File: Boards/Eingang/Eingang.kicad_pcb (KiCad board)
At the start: 2 copper layers, 9 parts, among them P1 CONN_01X02, P2 CONN_01X02, P3 CONN_01X02, P4 CONN_01X03, P5 CONN_01X03, P6 CONN_01X03, P7 CONN_01X02, P8 CONN_01X02, P9 CONN_01X02

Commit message: Layouting...
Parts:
- added REF**: EuroBoard_viertel_Type-II_100mmX40mm, EuroBoard_Outline:EuroBoard_viertel_Type-II_100mmX40mm, F.Cu at (90.2, 117.5)
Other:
- board outline added: 100 x 40 mm

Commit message: Work in Progress
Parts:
- P4, P5, P6: footprint Sockets_Mini-Universal:MiniUniversalMate-N-LokSocket_3PinVertical -> Connectors_Molex:Molex_MicroLatch-53253-0370_03x2.00mm_Straight
- moved P4 6.38 mm to (106.0, 92.7)
- moved P5 6.02 mm to (138.4, 92.7)
- moved P6 5.68 mm to (171.4, 92.7)
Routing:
- net Earth_Clean: track 240.2 -> 224.4 mm
- net Net-(P4-Pad3): track 27.4 -> 21.3 mm
- net Net-(P4-Pad1): track 26.1 -> 21.2 mm
- net Net-(P5-Pad3): track 26.2 -> 21.3 mm
- net Net-(P3-Pad1): track 25.9 -> 21.2 mm
- net Net-(P1-Pad1): track 25.6 -> 21.2 mm
- net Net-(P2-Pad1): track 25.6 -> 21.6 mm
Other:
- board text added: "Eingang"
- board text added: "V1.0 D. Walter"

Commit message: Work in Progress
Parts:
- removed P2, P7, P9: CONN_01X02, w_conn_av:rca_red
- removed P3, P8: CONN_01X02, w_conn_av:rca_black
- removed P4, P5: CONN_01X03, Connectors_Molex:Molex_MicroLatch-53253-0370_03x2.00mm_Straight
- removed REF**: EuroBoard_viertel_Type-II_100mmX40mm, EuroBoard_Outline:EuroBoard_viertel_Type-II_100mmX40mm
- added K1: DIP_7221-D, Reed:REED, F.Cu at (103.9, 94.0)
- added K2: DIP_7221-D, Reed:REED, F.Cu at (132.3, 94.0)
- added K4: DIP_7221-D, Reed:REED, F.Cu at (118.1, 94.0)
- added K5: DIP_7221-D, Reed:REED, F.Cu at (146.6, 94.0)
- added P10: BNC, w_conn_av:rca_red, F.Cu at (103.6, 112.3)
- added P11: BNC, w_conn_av:rca_white, F.Cu at (117.9, 112.3)
- added P12: BNC, w_conn_av:rca_red, F.Cu at (132.6, 112.3)
- added P13: BNC, w_conn_av:rca_white, F.Cu at (146.8, 112.3)
- P1: value CONN_01X02 -> CONN_01X04; footprint w_conn_av:rca_black -> Sockets_MOLEX_KK-System:Socket_MOLEX-KK-RM2-54mm_Lock_4pin_straight
- P6: footprint Connectors_Molex:Molex_MicroLatch-53253-0370_03x2.00mm_Straight -> Sockets_Mini-Universal:MiniUniversalMate-N-LokSocket_3PinVertical
- moved P6 36.4 mm to (137.7, 79.2)
- moved P1 17.2 mm to (165.1, 94.6)
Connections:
- P1 pad 1: Net-(P1-Pad1) -> Net-(K1-Pad2)
- P1 pad 2: Earth_Clean -> Net-(K2-Pad2)
- P6 pad 1: Net-(P1-Pad1) -> Net-(K1-Pad7)
- P6 pad 2: Earth_Clean -> Net-(K1-Pad14)
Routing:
- net Earth_Clean: track 224.4 -> 0.00 mm
- net Net-(K1-Pad7): track 0.00 -> 122.7 mm
- net Net-(K4-Pad7): track 21.6 -> 96.5 mm
- net Net-(K1-Pad14): track 0.00 -> 59.8 mm
- net Net-(K2-Pad2): track 0.00 -> 33.4 mm
- net Net-(K1-Pad2): track 0.00 -> 32.3 mm
- net Net-(K2-Pad1): track 0.00 -> 28.9 mm
- net Net-(K5-Pad1): track 0.00 -> 28.8 mm
- net Net-(K4-Pad1): track 0.00 -> 28.6 mm
- net Net-(K1-Pad1): track 0.00 -> 28.6 mm
- net Net-(P5-Pad3): track 21.3 -> 0.00 mm
- net Net-(P4-Pad3): track 21.3 -> 0.00 mm
- net Net-(P3-Pad1): track 21.2 -> 0.00 mm
- net Net-(P4-Pad1): track 21.2 -> 0.00 mm
- net Net-(P1-Pad1): track 21.2 -> 0.00 mm
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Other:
- board outline removed
- board text removed: "Eingang"
- board text removed: "V1.0 D. Walter"

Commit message: Work in Progress
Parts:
- removed P1: CONN_01X04, Sockets_MOLEX_KK-System:Socket_MOLEX-KK-RM2-54mm_Lock_4pin_straight
- added J1: Conn_01x02, Connectors_Molex:Molex_KK-6410-02_02x2.54mm_Straight, F.Cu at (133.3, 107.3)
- added J2: Conn_01x03, Connectors_Molex:Molex_KK-6410-03_03x2.54mm_Straight, F.Cu at (142.2, 107.3)
- added REF**: EuroBoard_viertel_Type-II_100mmX40mm_holes, EuroBoard_Outline:EuroBoard_viertel_Type-II_100mmX40mm_holes, F.Cu at (90.2, 117.5)
- P6: footprint Sockets_Mini-Universal:MiniUniversalMate-N-LokSocket_3PinVertical -> Connectors_Molex:Molex_KK-6410-03_03x2.54mm_Straight
- moved K2 43.6 mm to (175.9, 94.0), turned to 90 degrees
- moved P12 43.3 mm to (175.9, 112.3)
- moved K5 14.7 mm to (161.3, 94.0), turned to 90 degrees
- moved P13 14.5 mm to (161.3, 112.4)
- moved P6 12.8 mm to (141.6, 91.4), turned to 180 degrees
- turned K1 to 90 degrees
- turned K4 to 90 degrees
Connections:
- net Net-(K1-Pad6) renamed GND
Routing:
- net Net-(K4-Pad7): track 96.5 -> 56.2 mm
- net Net-(K1-Pad7): track 122.7 -> 84.4 mm, vias 0 -> 2
- net Net-(K1-Pad14): track 59.8 -> 92.2 mm
- net Net-(K5-Pad8): track 7.29 -> 37.0 mm, vias 0 -> 2
- net Net-(K1-Pad8): track 7.08 -> 36.6 mm
- net Net-(K4-Pad8): track 7.08 -> 34.8 mm, vias 0 -> 2
- net Net-(K2-Pad8): track 7.29 -> 34.4 mm, vias 0 -> 2
- net Net-(J1-Pad1): track 0.00 -> 22.0 mm
- net Net-(J2-Pad1): track 32.3 -> 45.3 mm
- net Net-(K2-Pad1): track 28.9 -> 17.8 mm
- net Net-(K5-Pad1): track 28.8 -> 18.0 mm
- net Net-(K1-Pad1): track 28.6 -> 17.8 mm
- net Net-(K4-Pad1): track 28.6 -> 18.1 mm
- net Net-(J2-Pad2): track 33.4 -> 43.6 mm
- added copper zone on B.Cu, net GND
- removed copper zone on B.Cu, net Earth_Clean
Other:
- board outline added: 100 x 40 mm

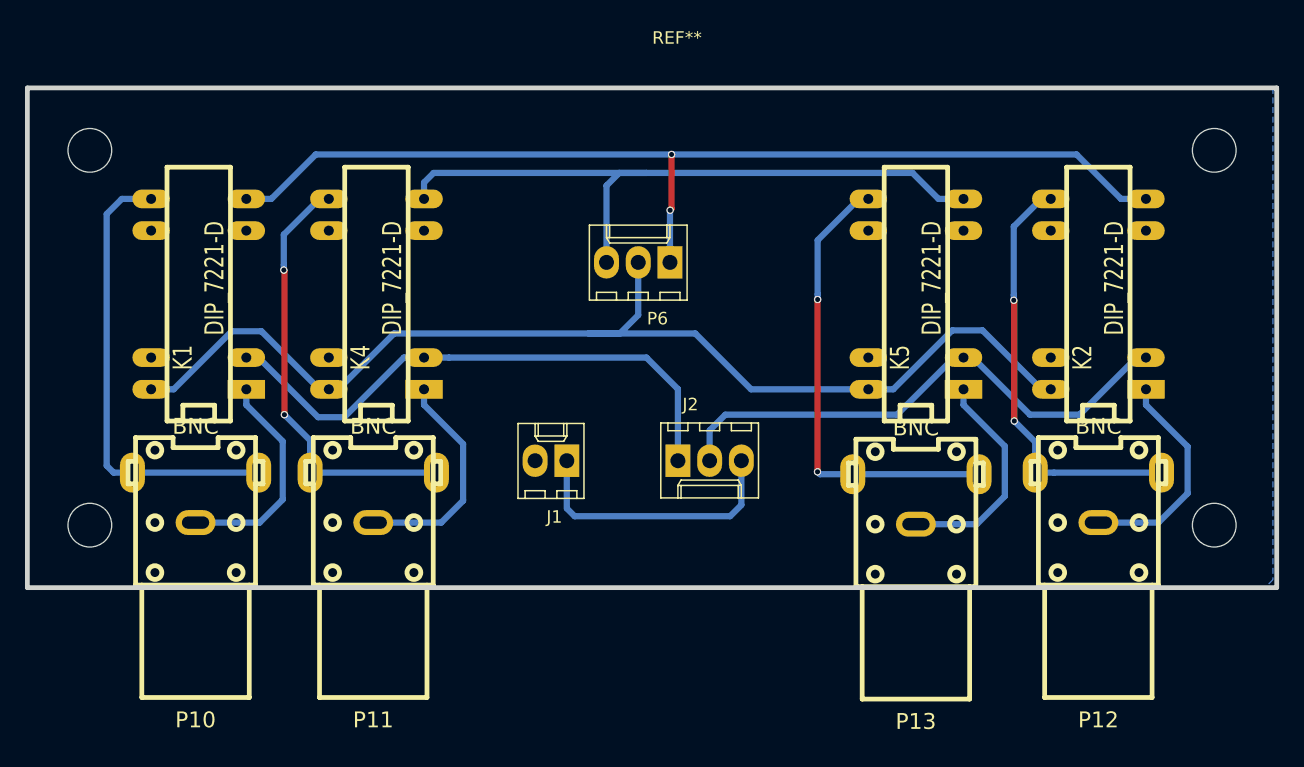
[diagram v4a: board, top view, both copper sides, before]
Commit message: Converted to Kicad 5.1 and Layout changes
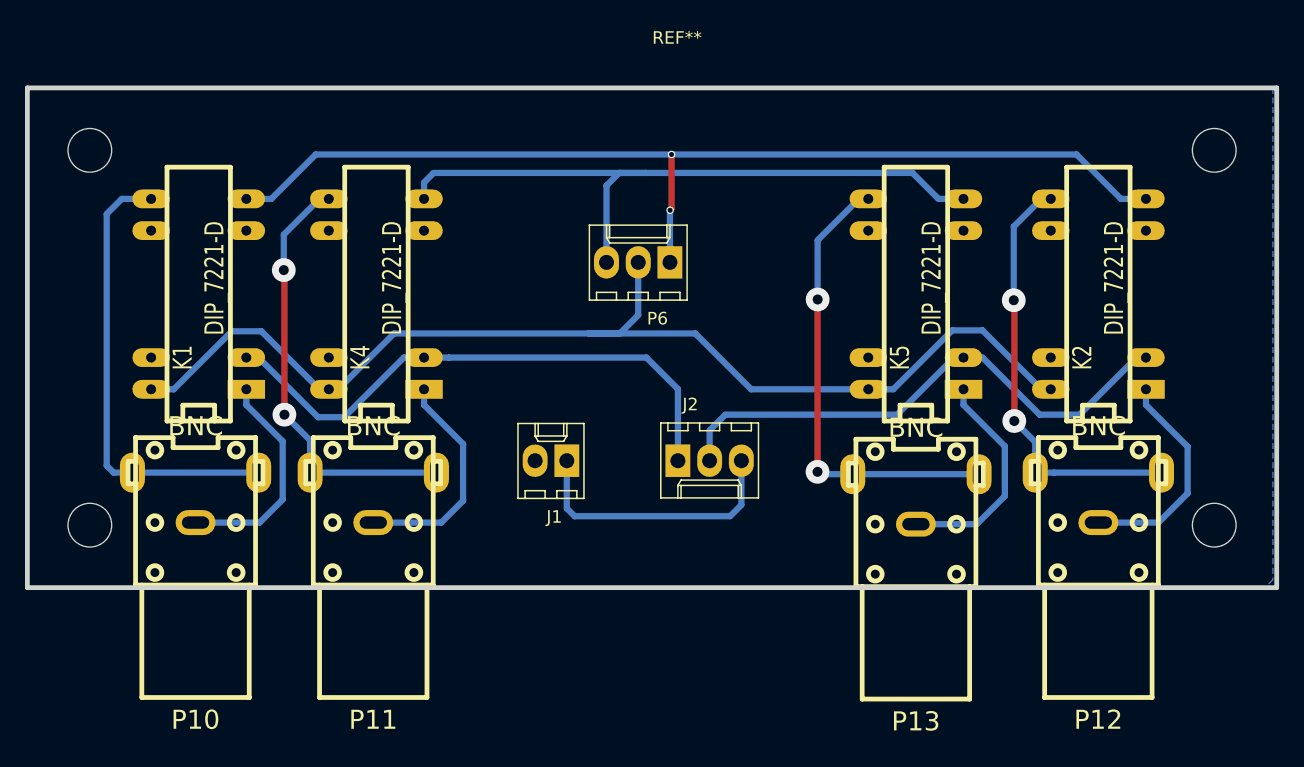
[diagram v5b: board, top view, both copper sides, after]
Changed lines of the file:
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@@
-(kicad_pcb (version 4) (host pcbnew 4.0.7)
+(kicad_pcb (version 20171130) (host pcbnew "(5.1.0)-1")
   (general
-    (links 29)
-    (no_connects 1)
-    (area 89.72 72.49958 190.560301 129.7654)
     (thickness 1.6)
     (drawings 0)
@@
   )
   (setup
-    (last_trace_width 0.5)
+    (last_trace_width 0.25)
     (user_trace_width 0.5)
     (user_trace_width 1)
@@
     (zone_45_only no)
     (trace_min 0.2)
-    (segment_width 0.2)
-    (edge_width 0.15)
     (via_size 0.6)
     (via_drill 0.4)
@@
     (uvia_min_size 0.2)
     (uvia_min_drill 0.1)
+    (edge_width 0.15)
+    (segment_width 0.2)
     (pcb_text_width 0.3)
     (pcb_text_size 1.5 1.5)
@@
       (layerselection 0x00030_80000001)
       (usegerberextensions false)
+      (usegerberattributes false)
+      (usegerberadvancedattributes false)
+      (creategerberjobfile false)
       (excludeedgelayer true)
       (linewidth 0.100000)
@@
       (hpglpennumber 1)
       (hpglpenspeed 20)
-      (hpglpendiameter 15)
-      (hpglpenoverlay 2)
+      (hpglpendiameter 15.000000)
       (psnegative false)
       (psa4output false)
@@
     (tags "rca, audio")
     (fp_text reference P10 (at 0 15.7988) (layer F.SilkS)
-      (effects (font (thickness 0.3048)))
+      (effects (font (size 1.524 1.524) (thickness 0.3048)))
     )
     (fp_text value BNC (at 0 -7.69874) (layer F.SilkS)
-      (effects (font (thickness 0.3048)))
+      (effects (font (size 1.524 1.524) (thickness 0.3048)))
     )
     (fp_circle (center -3.2512 -5.79882) (end -3.79984 -5.79882) (layer F.SilkS) (width 0.381))
@@
     (tags "rca, audio")
     (fp_text reference P11 (at 0 15.7988) (layer F.SilkS)
-      (effects (font (thickness 0.3048)))
+      (effects (font (size 1.524 1.524) (thickness 0.3048)))
     )
     (fp_text value BNC (at 0 -7.69874) (layer F.SilkS)
-      (effects (font (thickness 0.3048)))
+      (effects (font (size 1.524 1.524) (thickness 0.3048)))
     )
     (fp_circle (center -3.2512 -5.79882) (end -3.79984 -5.79882) (layer F.SilkS) (width 0.381))
@@
     (tags "rca, audio")
     (fp_text reference P12 (at 0 15.7988) (layer F.SilkS)
-      (effects (font (thickness 0.3048)))
+      (effects (font (size 1.524 1.524) (thickness 0.3048)))
     )
     (fp_text value BNC (at 0 -7.69874) (layer F.SilkS)
-      (effects (font (thickness 0.3048)))
+      (effects (font (size 1.524 1.524) (thickness 0.3048)))
     )
     (fp_circle (center -3.2512 -5.79882) (end -3.79984 -5.79882) (layer F.SilkS) (width 0.381))
@@
     (tags "rca, audio")
     (fp_text reference P13 (at 0 15.7988) (layer F.SilkS)
-      (effects (font (thickness 0.3048)))
+      (effects (font (size 1.524 1.524) (thickness 0.3048)))
     )
     (fp_text value BNC (at 0 -7.69874) (layer F.SilkS)
-      (effects (font (thickness 0.3048)))
+      (effects (font (size 1.524 1.524) (thickness 0.3048)))
     )
     (fp_circle (center -3.2512 -5.79882) (end -3.79984 -5.79882) (layer F.SilkS) (width 0.381))
@@
   (segment (start 171.3357 86.36) (end 169.121856 88.573844) (width 0.5) (layer B.Cu) (net 6))
   (segment (start 172.085 86.36) (end 171.3357 86.36) (width 0.5) (layer B.Cu) (net 6))
-  (via (at 169.121856 94.471614) (size 0.6) (drill 0.4) (layers F.Cu B.Cu) (net 6))
+  (via (at 169.121856 94.471614) (size 1.9) (drill 0.8) (layers F.Cu B.Cu) (net 6))
   (segment (start 170.8404 108.27004) (end 170.8404 105.8164) (width 0.5) (layer B.Cu) (net 6))
   (segment (start 170.8404 105.8164) (end 169.164 104.14) (width 0.5) (layer B.Cu) (net 6))
-  (via (at 169.164 104.14) (size 0.6) (drill 0.4) (layers F.Cu B.Cu) (net 6))
+  (via (at 169.164 104.14) (size 1.9) (drill 0.8) (layers F.Cu B.Cu) (net 6))
   (segment (start 170.8404 108.27004) (end 172.33989 108.27004) (width 0.5) (layer B.Cu) (net 6))
   (segment (start 172.33989 108.27004) (end 180.9496 108.27004) (width 0.5) (layer B.Cu) (net 6))
@@
   (segment (start 114.3 86.36) (end 113.5507 86.36) (width 0.5) (layer B.Cu) (net 9))
   (segment (start 110.695682 91.632875) (end 110.695682 92.057139) (width 0.5) (layer B.Cu) (net 9))
-  (via (at 110.695682 92.057139) (size 0.6) (drill 0.4) (layers F.Cu B.Cu) (net 9))
+  (via (at 110.695682 92.057139) (size 1.9) (drill 0.8) (layers F.Cu B.Cu) (net 9))
   (segment (start 112.8014 108.27004) (end 112.8014 105.6894) (width 0.5) (layer B.Cu) (net 9))
   (segment (start 112.8014 105.6894) (end 110.744 103.632) (width 0.5) (layer B.Cu) (net 9))
-  (via (at 110.744 103.632) (size 0.6) (drill 0.4) (layers F.Cu B.Cu) (net 9))
+  (via (at 110.744 103.632) (size 1.9) (drill 0.8) (layers F.Cu B.Cu) (net 9))
   (segment (start 122.9106 108.27004) (end 112.8014 108.27004) (width 0.5) (layer B.Cu) (net 9))
   (segment (start 161.29 112.395) (end 166.165624 112.395) (width 0.5) (layer B.Cu) (net 10))
@@
   (segment (start 157.48 86.36) (end 156.7307 86.36) (width 0.5) (layer B.Cu) (net 11))
   (segment (start 153.426007 89.664693) (end 153.426007 93.988343) (width 0.5) (layer B.Cu) (net 11))
-  (via (at 153.426007 94.412607) (size 0.6) (drill 0.4) (layers F.Cu B.Cu) (net 11))
+  (via (at 153.426007 94.412607) (size 1.9) (drill 0.8) (layers F.Cu B.Cu) (net 11))
   (segment (start 156.2354 108.39704) (end 153.60904 108.39704) (width 0.5) (layer B.Cu) (net 11))
   (segment (start 153.60904 108.39704) (end 153.416 108.204) (width 0.5) (layer B.Cu) (net 11))
-  (via (at 153.416 108.204) (size 0.6) (drill 0.4) (layers F.Cu B.Cu) (net 11))
+  (via (at 153.416 108.204) (size 1.9) (drill 0.8) (layers F.Cu B.Cu) (net 11))
   (segment (start 156.2354 108.39704) (end 166.3446 108.39704) (width 0.5) (layer B.Cu) (net 11))
   (segment (start 133.35 107.315) (end 133.35 111.130499) (width 0.5) (layer B.Cu) (net 12))
@@
   (segment (start 159.7787 103.632) (end 164.3507 99.06) (width 0.5) (layer B.Cu) (net 15))
   (segment (start 164.3507 99.06) (end 165.1 99.06) (width 0.5) (layer B.Cu) (net 15))
-  (segment (start 170.4213 103.632) (end 174.3837 103.632) (width 0.5) (layer B.Cu) (net 15))
+  (segment (start 178.9557 99.06) (end 179.705 99.06) (width 0.5) (layer B.Cu) (net 15))
   (segment (start 174.3837 103.632) (end 178.9557 99.06) (width 0.5) (layer B.Cu) (net 15))
-  (segment (start 178.9557 99.06) (end 179.705 99.06) (width 0.5) (layer B.Cu) (net 15))
-  (segment (start 165.1 99.06) (end 165.8493 99.06) (width 0.5) (layer B.Cu) (net 15))
-  (segment (start 165.8493 99.06) (end 170.4213 103.632) (width 0.5) (layer B.Cu) (net 15))
+  (segment (start 171.196 103.632) (end 174.3837 103.632) (width 0.5) (layer B.Cu) (net 15))
+  (segment (start 165.1 99.06) (end 166.624 99.06) (width 0.5) (layer B.Cu) (net 15))
+  (segment (start 166.624 99.06) (end 171.196 103.632) (width 0.5) (layer B.Cu) (net 15))
   (zone (net 13) (net_name GND) (layer B.Cu) (hatch edge 0.508)
     (connect_pads (clearance 0.508))

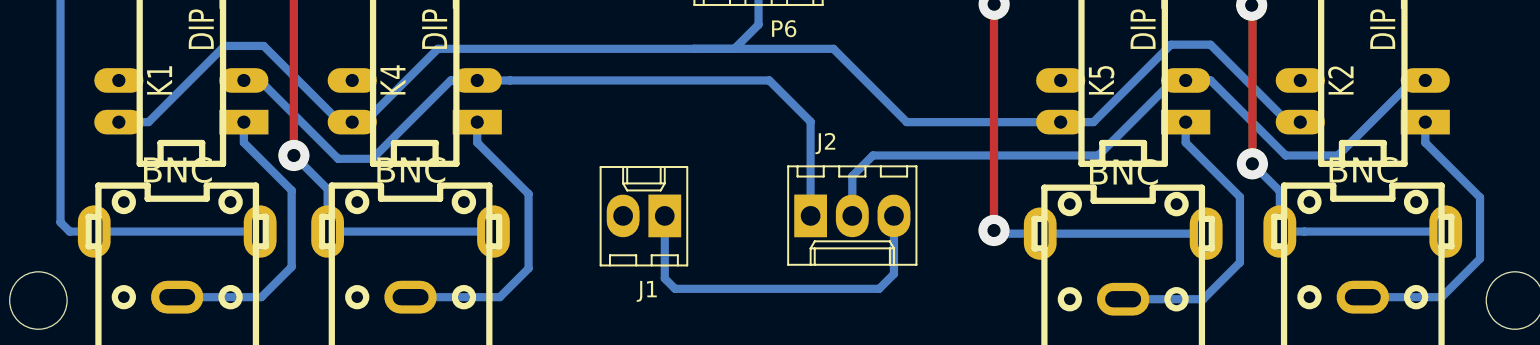
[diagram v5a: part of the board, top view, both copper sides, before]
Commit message: Layout changes after migrate to Kicad 5.1
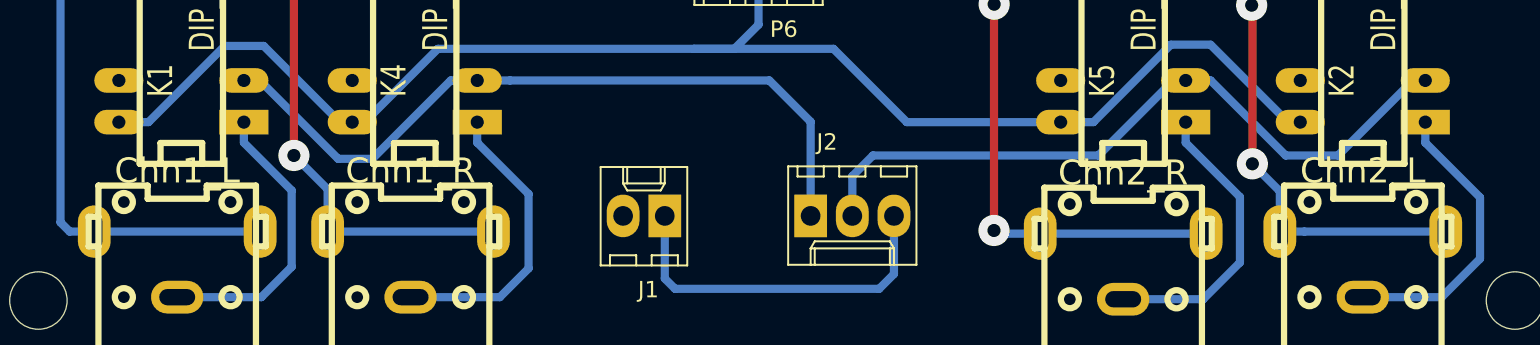
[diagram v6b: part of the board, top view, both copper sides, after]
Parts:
- J1: value Conn_01x02 -> 12V_Sup
- J2: value Conn_01x03 -> Chn_Switch
- P10: value BNC -> Chn1_L
- P11: value BNC -> Chn1_R
- P12: value BNC -> Chn2_L
- P13: value BNC -> Chn2_R
- P6: value CONN_01X03 -> LF_Out
